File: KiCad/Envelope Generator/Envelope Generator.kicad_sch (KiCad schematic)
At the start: 34 parts, among them U10 TL074, U9 TL074

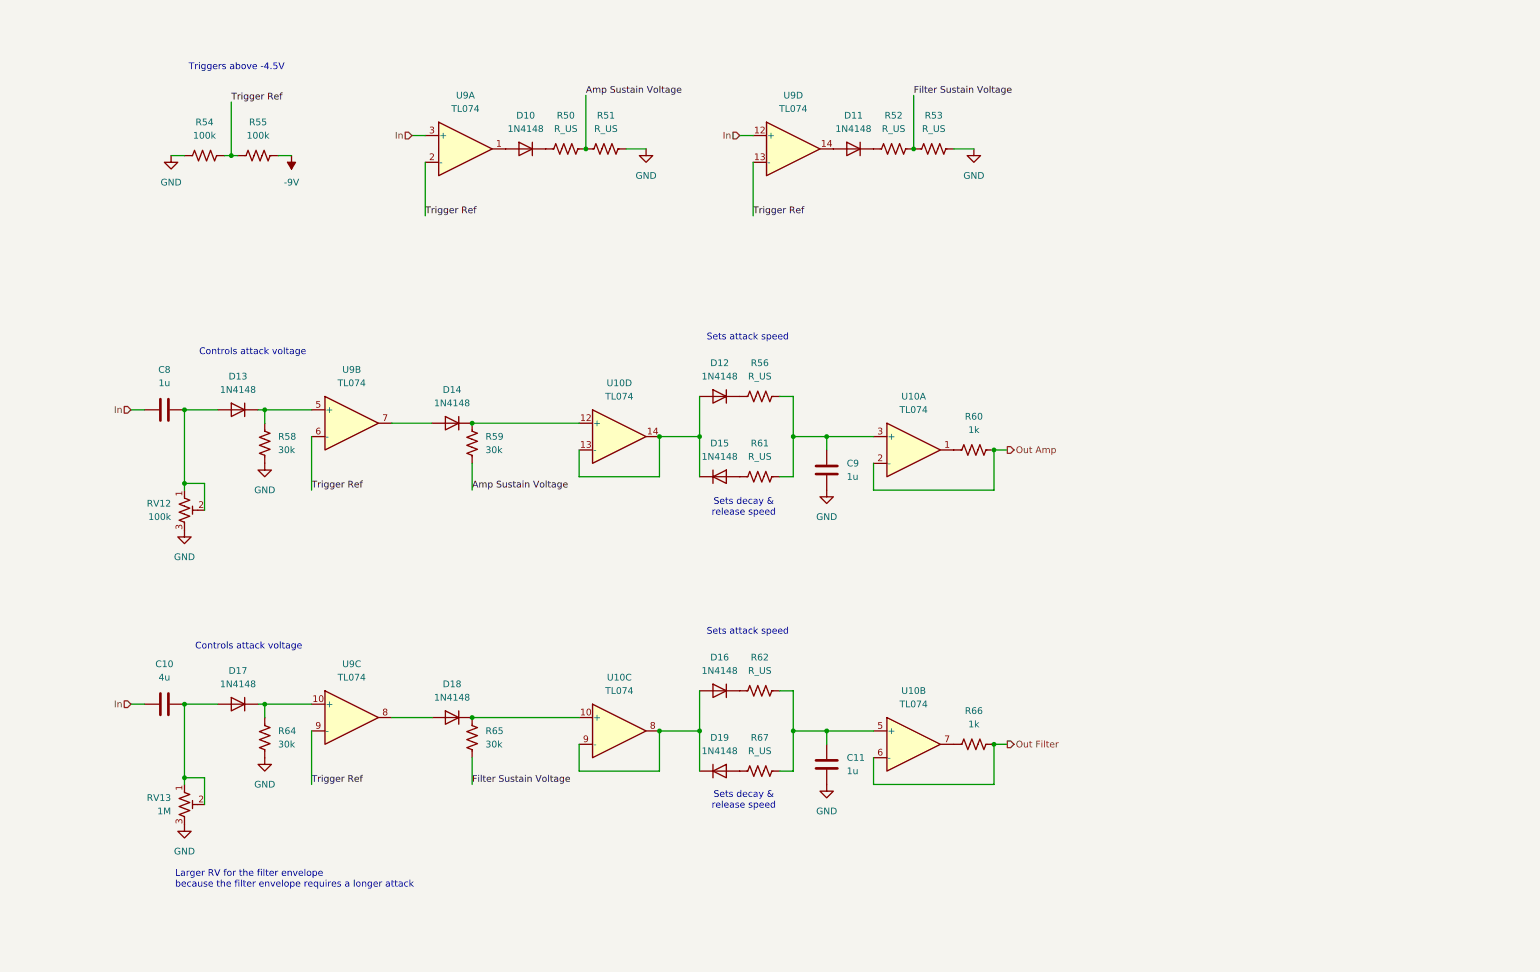
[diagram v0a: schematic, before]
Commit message: started separating into different boards, partially fixed envelope generator
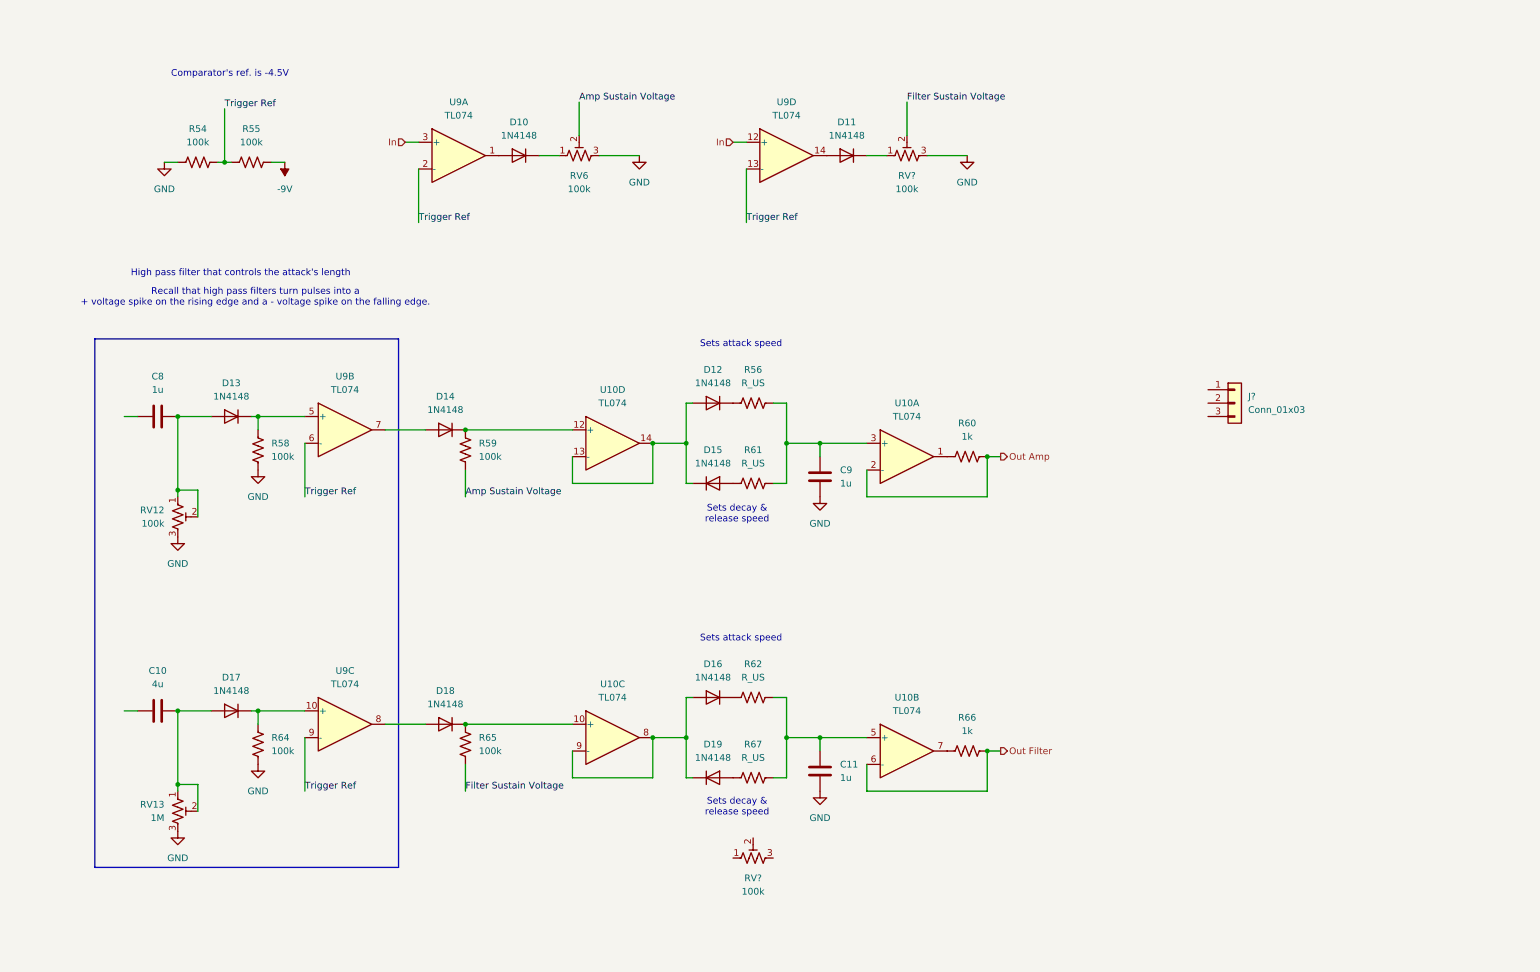
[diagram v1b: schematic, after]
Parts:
- removed R50, R51, R52, R53: R_US, Resistor_THT:R_Axial_DIN0207_L6.3mm_D2.5mm_P7.62mm_Horizontal, symbol Device:R_US
- added J?: Conn_01x03, symbol Connector_Generic:Conn_01x03
- added RV6, RV?: 100k, Potentiometer_SMD:Potentiometer_Bourns_TC33X_Vertical, symbol Device:R_Potentiometer_Trim_US
- added RV?: 100k, symbol Device:R_Potentiometer_Trim_US
- R58, R59, R64, R65: value 30k -> 100k
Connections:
- net Amp Sustain Voltage: now also RV6.2
- net Filter Sustain Voltage: now also RV?.2
- net GND: now also RV6.3, RV?.3
- net In: no longer C10.1, C8.1
- net at D11.1 (K): now also RV?.1
- net at D10.1 (K): now also RV6.1
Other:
- note added: "Comparator's ref. is -4.5V"
- note added: "High pass filter that controls the attack's length"
- note added: "Recall that high pass filters turn pulses into a + voltage spike on the rising edge and a - voltage spike on the falling edge."
- note removed: "Controls attack voltage"
- note removed: "Larger RV for the filter envelope because the filter envelope requires a longer attack"
- note removed: "Triggers above -4.5V"
- moved on the sheet: C10, C11, C8, C9, D10, D11, D12, D13, D14, D15, D16, D17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

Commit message: fixed envelope generator
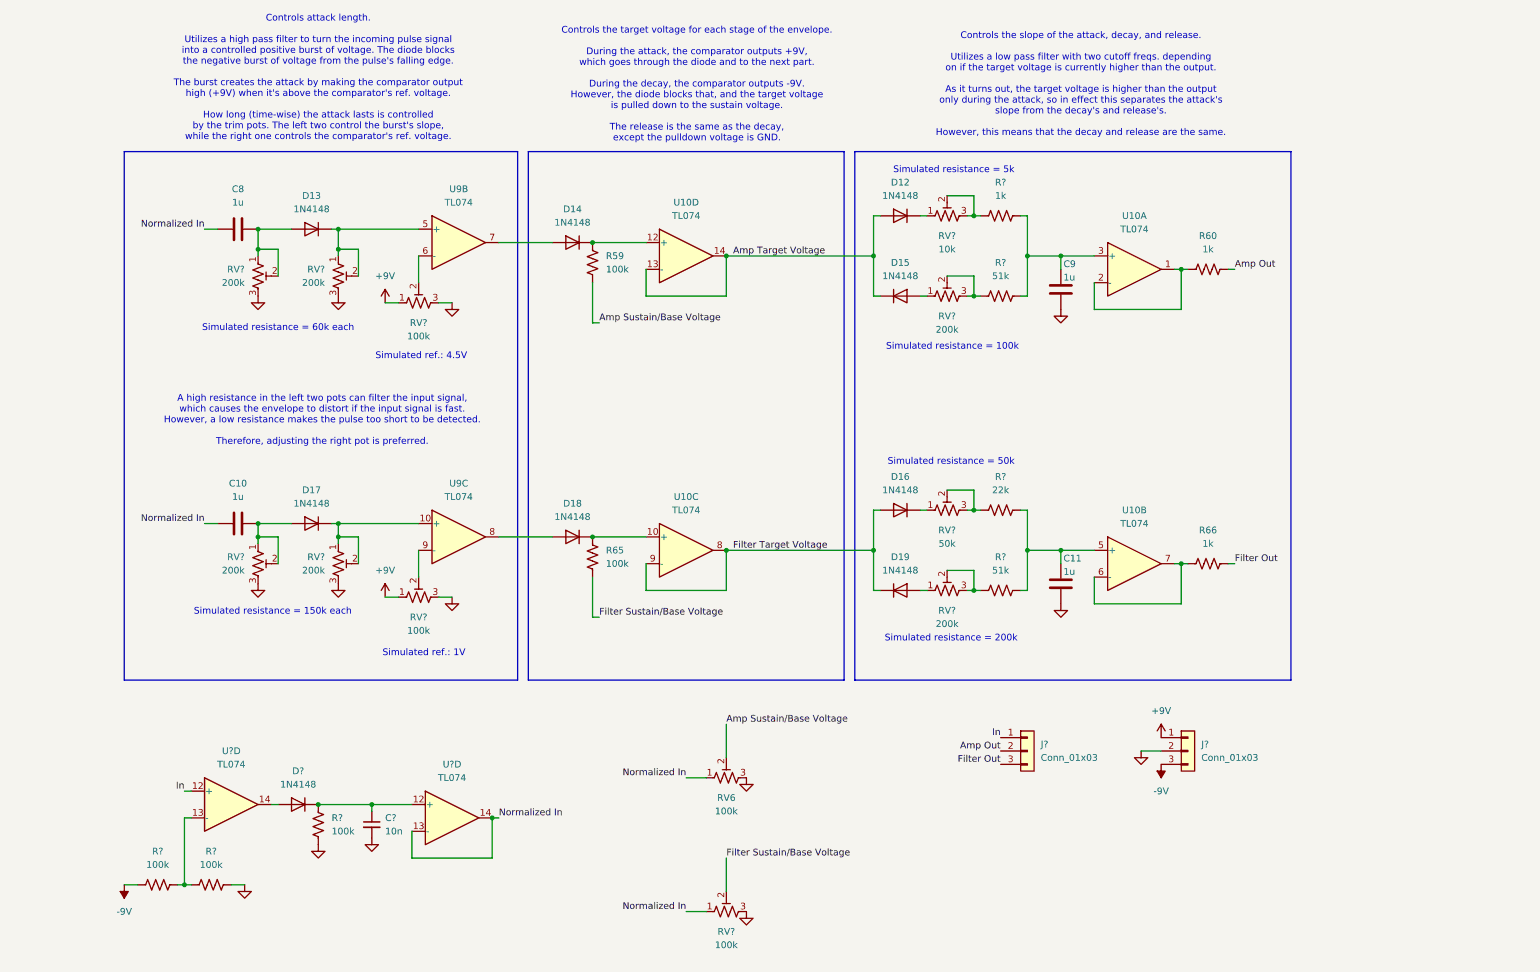
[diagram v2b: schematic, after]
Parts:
- removed D10, D11: 1N4148, Diode_THT:D_DO-35_SOD27_P7.62mm_Horizontal, symbol Diode:1N4148
- removed R54, R55, R58, R64: 100k, Resistor_SMD:R_0603_1608Metric, symbol Device:R_US
- removed R56, R61, R62, R67: R_US, Resistor_THT:R_Axial_DIN0207_L6.3mm_D2.5mm_P7.62mm_Horizontal, symbol Device:R_US
- removed RV12: 100k, Potentiometer_THT:Potentiometer_Bourns_3296W_Vertical, symbol Device:R_Potentiometer_Trim_US
- removed RV13: 1M, Potentiometer_THT:Potentiometer_Bourns_3296W_Vertical, symbol Device:R_Potentiometer_Trim_US
- removed RV?: 100k, symbol Device:R_Potentiometer_Trim_US
- removed unit 1 of U9
- removed unit 4 of U9
- added C?: 10n, symbol Device:C_Small
- added D?: 1N4148, Diode_THT:D_DO-35_SOD27_P7.62mm_Horizontal, symbol Diode:1N4148
- added J?: Conn_01x03, symbol Connector_Generic:Conn_01x03
- added R?: 1k, symbol Device:R_US
- added R? (x3): 100k, symbol Device:R_US
- added R?: 22k, symbol Device:R_US
- added R? (x2): 51k, symbol Device:R_US
- added RV? (x2): 100k, Potentiometer_THT:Potentiometer_Bourns_3296W_Vertical, symbol Device:R_Potentiometer_Trim_US
- added RV? (x6): 200k, symbol Device:R_Potentiometer_Trim_US
- added RV?: 10k, symbol Device:R_Potentiometer_Trim_US
- added RV?: 50k, symbol Device:R_Potentiometer_Trim_US
- added U? (x2): TL074, Package_DIP:DIP-14_W7.62mm, symbol Amplifier_Operational:TL074
- C10: value 4u -> 1u
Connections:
- net -9V: now also J?.3 (Pin_3), R?.1
- net GND: now also C?.2, J?.2 (Pin_2), R?.2, R?.2, RV?.3, RV?.3, RV?.3, RV?.3, RV?.3, RV?.3
- net In: now also J?.1 (Pin_1), U?.12 (+)
- net at D19.2 (A): now also RV?.1
- net at C11.2, U10.5 (+): now also R?.2, R?.2
- net at C9.2, U10.3 (+): now also R?.2, R?.2
- net Normalized In: now reaches RV6.1
- net Normalized In: now also C10.1, C8.1, RV?.1, U?.13 (-), U?.14
- net at C10.2, D17.2 (A): now also RV?.1, RV?.2
- net at R66.1, U10.7: now also U10.6 (-)
- net at D12.1 (K): now also RV?.1
- net at D13.1 (K), U9.5 (+): now also RV?.1, RV?.2
- net Filter Target Voltage: now reaches D16.2 (A), D19.1 (K), U10.8, U10.9 (-)
- net Amp Target Voltage: now reaches D12.2 (A), D15.1 (K), U10.13 (-), U10.14
- net at C8.2, D13.2 (A): now also RV?.1, RV?.2
- net at D17.1 (K), U9.10 (+): now also RV?.1, RV?.2
- net at R60.1, U10.1: now also U10.2 (-)
- net at D15.2 (A): now also RV?.1
- net at D16.1 (K): now also RV?.1
- net Amp Out: now reaches J?.2 (Pin_2)
- net Amp Out: now also R60.2
- net Filter Out: now reaches J?.3 (Pin_3)
- net Filter Out: now also R66.2
- net Amp Sustain Voltage renamed Amp Sustain/Base Voltage
- net Filter Sustain Voltage renamed Filter Sustain/Base Voltage
- removed net Out Amp: R60.2, U10.2 (-)
- removed net Out Filter: R66.2, U10.6 (-)
- net Trigger Ref: no longer names the net of U9.9 (-)
- net Trigger Ref: now also RV?.2; no longer U9.6 (-)
- new net: R?.1, RV?.2, RV?.3 (x4)
- new net: R?.1, R?.2, U?.13 (-)
- new net: C?.1, D?.1 (K), R?.1, U?.12 (+)
- new net: D?.2 (A), U?.14
- new net: RV?.2, U9.6 (-)
- new net +9V: J?.1 (Pin_1), RV?.1, RV?.1
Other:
- note added: "A high resistance in the left two pots can filter the input signal, which causes the envelope to distort if the input signal is fast. However, a low resistance makes the pulse too short to be detected. Therefore, adjusting the right pot is preferred."
- note added: "Controls attack length. Utilizes a high pass filter to turn the incoming pulse signal into a controlled positive burst of voltage. The diode blocks the negative burst of voltage from the pulse's falling edge. The burst creates the attack by making the comparator output high (+9V) when it's above the comparator's ref. voltage. How long (time-wise) the attack lasts is controlled by the trim pots. T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"
- note added: "Controls the slope of the attack, decay, and release. Utilizes a low pass filter with two cutoff freqs. depending on if the target voltage is currently higher than the output. As it turns out, the target voltage is higher than the output only during the attack, so in effect this separates the attack's slope from the decay's and release's. However, this means that the decay and release are the sam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"
- note added: "Controls the target voltage for each stage of the envelope. During the attack, the comparator outputs +9V, which goes through the diode and to the next part. During the decay, the comparator outputs -9V. However, the diode blocks that, and the target voltage is pulled down to the sustain voltage. The release is the same as the decay, except the pulldown voltage is GND."
- note added: "Simulated ref.: 1V"
- note added: "Simulated ref.: 4.5V"
- note added: "Simulated resistance = 100k"
- note added: "Simulated resistance = 150k each"
- note added: "Simulated resistance = 200k"
- note added: "Simulated resistance = 50k"
- note added: "Simulated resistance = 5k"
- note added: "Simulated resistance = 60k each"
- note removed: "Comparator's ref. is -4.5V"
- note removed: "High pass filter that controls the attack's length"
- note removed: "Recall that high pass filters turn pulses into a + voltage spike on the rising edge and a - voltage spike on the falling edge."
- note removed: "Sets attack speed"
- note removed: "Sets decay & release speed"
- moved on the sheet: C10, C11, C8, C9, D12, D13, D14, D15, D16, D17, D18, D19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

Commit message: completed envelope generator schematic
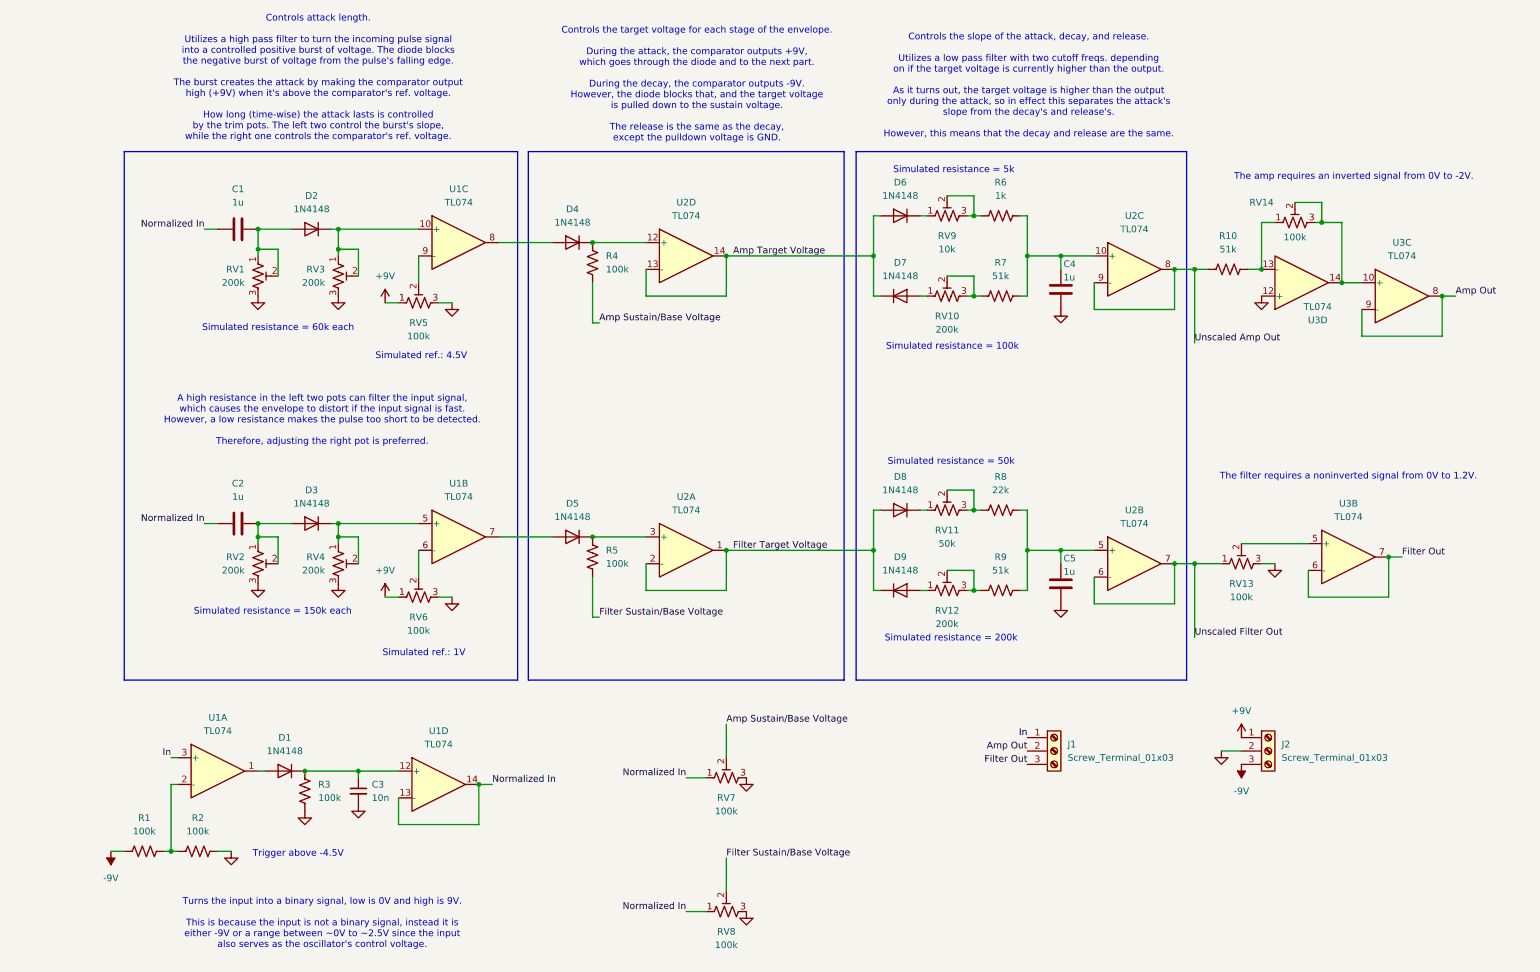
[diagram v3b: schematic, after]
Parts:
- removed J? (x2): Conn_01x03, symbol Connector_Generic:Conn_01x03
- removed R60, R66: 1k, Resistor_SMD:R_0603_1608Metric, symbol Device:R_US
- added J1, J2: Screw_Terminal_01x03, symbol Connector:Screw_Terminal_01x03
- added R10: 51k, symbol Device:R_US
- added RV13, RV14: 100k, symbol Device:R_Potentiometer_Trim_US
- added U3: TL074, Package_DIP:DIP-14_W7.62mm, symbol Amplifier_Operational:TL074
- gave numbers to parts that had none: 21
- renumbered C8 to C1, C10 to C2, C9 to C4, C11 to C5, D13 to D2, D17 to D3, D14 to D4, D18 to D5, D12 to D6, D15 to D7, D16 to D8, D19 to D9, R59 to R4, R65 to R5, RV6 to RV7, U9 to U1, U10 to U2
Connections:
- net +9V: now also J2.1 (Pin_1)
- net -9V: now also J2.3 (Pin_3)
- net Amp Out: now also J1.2 (Pin_2), U3.8, U3.9 (-)
- net Filter Out: now also J1.3 (Pin_3), U3.6 (-), U3.7
- net Filter Target Voltage: now also U2.1, U2.2 (-); no longer U2.8, U2.9 (-)
- net GND: now also J2.2 (Pin_2), RV13.3, U3.12 (+)
- net In: now also U1.3 (+), J1.1 (Pin_1); no longer U1.12 (+)
- net at C4.2, R6.2, R7.2: now also U2.10 (+); no longer U2.3 (+)
- net at RV6.2: now also U1.6 (-); no longer U1.9 (-)
- net at D5.1 (K), R5.1: now also U2.3 (+); no longer U2.10 (+)
- net at D5.2 (A): now also U1.7; no longer U1.8
- net Unscaled Filter Out: now reaches U2.6 (-), U2.7
- net Unscaled Filter Out: now also RV13.1
- net at R1.2, R2.1: now also U1.2 (-); no longer U1.13 (-)
- net at D2.1 (K), RV3.1, RV3.2: now also U1.10 (+); no longer U1.5 (+)
- net at D3.1 (K), RV4.1, RV4.2: now also U1.5 (+); no longer U1.10 (+)
- net at D1.2 (A): now also U1.1; no longer U1.14
- net at RV5.2: now also U1.9 (-); no longer U1.6 (-)
- net at D4.2 (A): now also U1.8; no longer U1.7
- new net: RV13.2, U3.5 (+)
- new net: R10.2, RV14.1, U3.13 (-)
- new net: RV14.2, RV14.3, U3.10 (+), U3.14
- new net Unscaled Amp Out: R10.1, U2.8, U2.9 (-)
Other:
- note added: "The amp requires an inverted signal from 0V to -2V."
- note added: "The filter requires a noninverted signal from 0V to 1.2V."
- note added: "Trigger above -4.5V"
- note added: "Turns the input into a binary signal, low is 0V and high is 9V. This is because the input is not a binary signal, instead it is either -9V or a range between ~0V to ~2.5V since the input also serves as the oscillator's control voltage."
- moved on the sheet: C3, D1, R1, R2, R3, U1A, U1D
